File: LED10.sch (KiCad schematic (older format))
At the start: 2 parts

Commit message: initial layout
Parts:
- renumbered R1801 to R1601, R1802 to R1602
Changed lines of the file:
@@
 	7900 3850 8250 3850
 $Comp
-L Device:R_Small_US R1801
+L Device:R_Small_US R1601
 U 1 1 61A1E529
 P 3650 3200
-F 0 "R1801" V 3445 3200 50  0000 C CNN
+F 0 "R1601" V 3445 3200 50  0000 C CNN
 F 1 "150 5%" V 3536 3200 50  0000 C CNN
 F 2 "Resistor_SMD:R_0805_2012Metric_Pad1.20x1.40mm_HandSolder" H 3650 3200 50  0001 C CNN
@@
 	3300 3200 3550 3200
 $Comp
-L Device:R_Small_US R1802
+L Device:R_Small_US R1602
 U 1 1 61A20FA6
 P 9300 3850
-F 0 "R1802" V 9095 3850 50  0000 C CNN
+F 0 "R1602" V 9095 3850 50  0000 C CNN
 F 1 "2.7k 5%" V 9186 3850 50  0000 C CNN
 F 2 "Resistor_SMD:R_0805_2012Metric_Pad1.20x1.40mm_HandSolder" H 9300 3850 50  0001 C CNN
@@
 	8900 3850 9200 3850
 $Comp
-L power:GND #PWR01801
+L power:GND #PWR01601
 U 1 1 61A21A87
 P 9700 4000
-F 0 "#PWR01801" H 9700 3750 50  0001 C CNN
+F 0 "#PWR01601" H 9700 3750 50  0001 C CNN
 F 1 "GND" H 9705 3827 50  0000 C CNN
 F 2 "" H 9700 4000 50  0001 C CNN

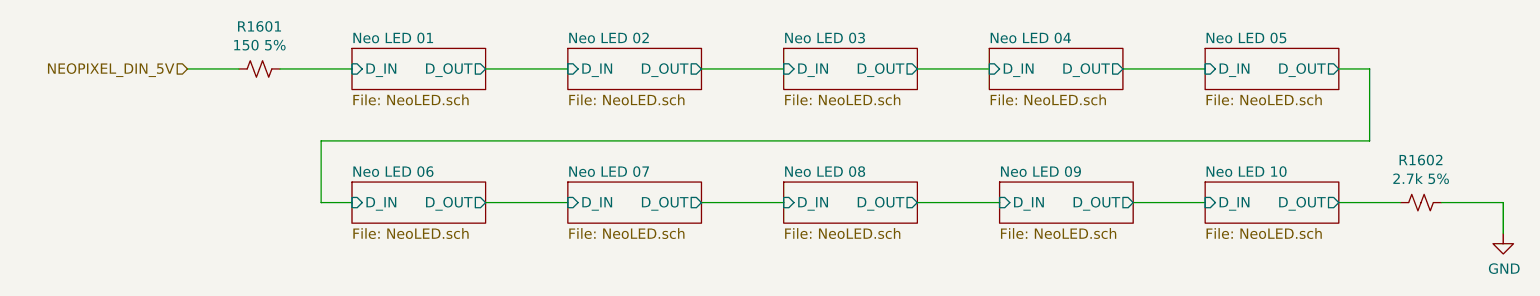
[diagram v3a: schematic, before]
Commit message: Fix design error in PI4ULS5V201TAEX. Reset and reassigned all annotations.
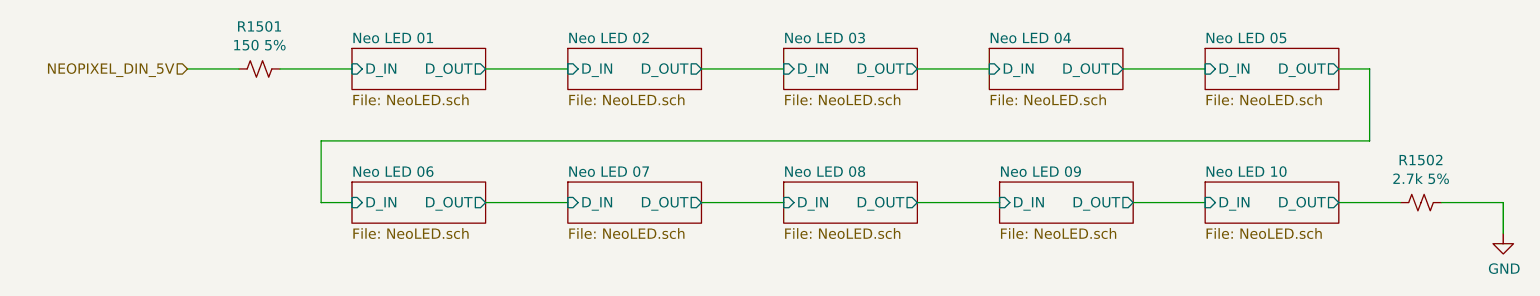
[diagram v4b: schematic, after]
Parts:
- renumbered R1601 to R1501, R1602 to R1502
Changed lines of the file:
@@
 	7900 3850 8250 3850
 $Comp
-L Device:R_Small_US R1601
+L Device:R_Small_US R1501
 U 1 1 61A1E529
 P 3650 3200
-F 0 "R1601" V 3445 3200 50  0000 C CNN
+F 0 "R1501" V 3445 3200 50  0000 C CNN
 F 1 "150 5%" V 3536 3200 50  0000 C CNN
 F 2 "Resistor_SMD:R_0805_2012Metric_Pad1.20x1.40mm_HandSolder" H 3650 3200 50  0001 C CNN
@@
 	3300 3200 3550 3200
 $Comp
-L Device:R_Small_US R1602
+L Device:R_Small_US R1502
 U 1 1 61A20FA6
 P 9300 3850
-F 0 "R1602" V 9095 3850 50  0000 C CNN
+F 0 "R1502" V 9095 3850 50  0000 C CNN
 F 1 "2.7k 5%" V 9186 3850 50  0000 C CNN
 F 2 "Resistor_SMD:R_0805_2012Metric_Pad1.20x1.40mm_HandSolder" H 9300 3850 50  0001 C CNN
@@
 	8900 3850 9200 3850
 $Comp
-L power:GND #PWR01601
+L power:GND #PWR01501
 U 1 1 61A21A87
 P 9700 4000
-F 0 "#PWR01601" H 9700 3750 50  0001 C CNN
+F 0 "#PWR01501" H 9700 3750 50  0001 C CNN
 F 1 "GND" H 9705 3827 50  0000 C CNN
 F 2 "" H 9700 4000 50  0001 C CNN
